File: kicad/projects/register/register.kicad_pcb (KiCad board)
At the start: 2 copper layers, 165.1 x 50.8 mm, 22 parts, among them J1 LEFT IN, J10 RIGHT LEDS, J2 LEFT OUT, J3 LEFT CONTENT, J4 BUS, J5 LEFT LEDS, J6 BACKPLANE, J7 RIGHT IN, J8 RIGHT OUT, J9 RIGHT CONTENT, U1 74HCT377, U2 74HCT245, U3 74HCT377, U4 74HCT245, U5 74HCT04

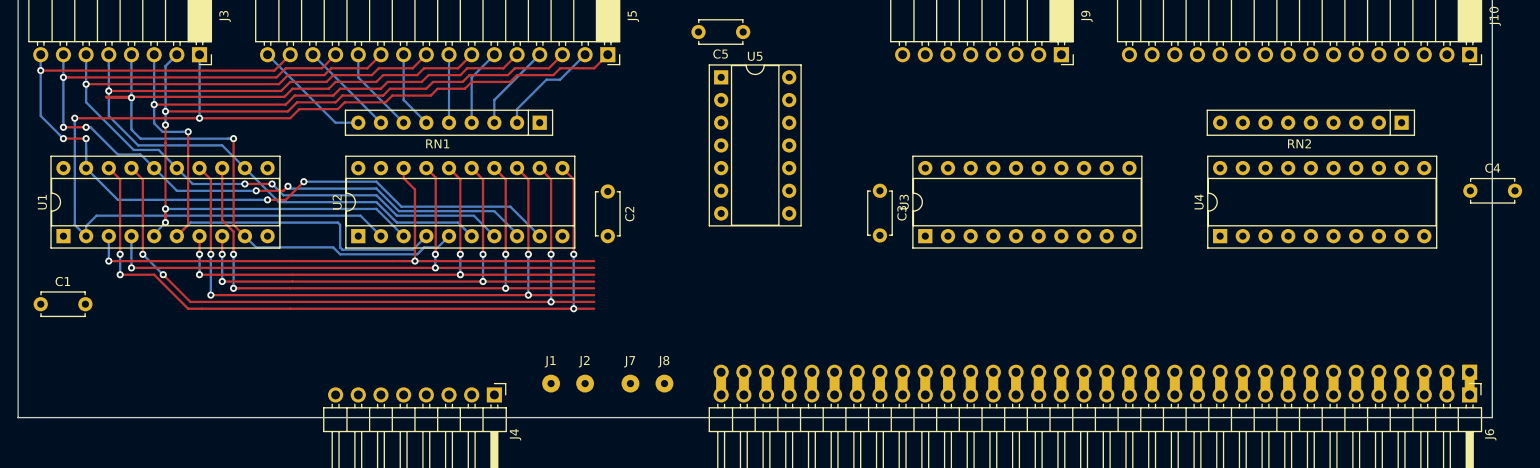
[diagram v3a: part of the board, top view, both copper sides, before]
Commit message: Add power and control signals.
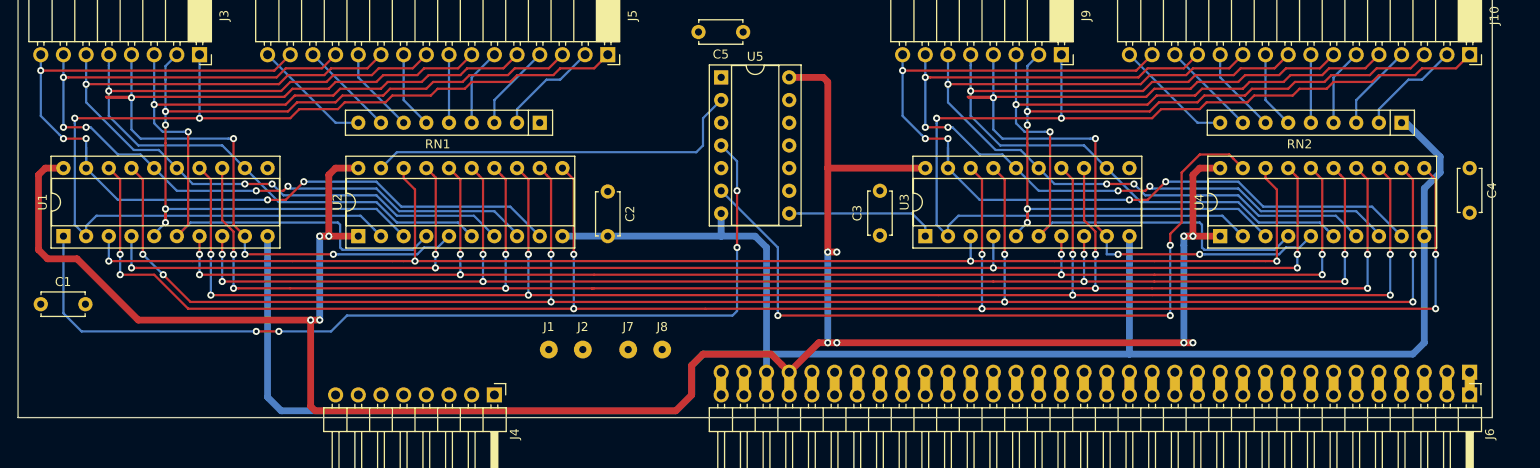
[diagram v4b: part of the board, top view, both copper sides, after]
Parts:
- moved J7 3.82 mm to (131.8, 119.4)
- moved J2 3.82 mm to (126.7, 119.4)
- moved J1 3.82 mm to (122.9, 119.4)
- moved J8 3.82 mm to (135.6, 119.4)
- moved C4 2.54 mm to (226.1, 99.1), turned to 270 degrees
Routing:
- net VCC: track 0.00 -> 259.8 mm, vias 0 -> 12
- net GND: track 0.00 -> 233.9 mm
- net /BUS_7: track 83.4 -> 210.2 mm, vias 4 -> 8
- net /BUS_6: track 78.4 -> 201.2 mm, vias 4 -> 8
- net Net-(J10-Pad1): track 0.00 -> 119.1 mm, vias 0 -> 2
- net /BUS_5: track 72.4 -> 191.1 mm, vias 4 -> 8
- net /BUS_4: track 68.4 -> 183.2 mm, vias 4 -> 8
- net Net-(U1-Pad1): track 0.00 -> 105.1 mm, vias 0 -> 4
- net Net-(J10-Pad7): track 0.00 -> 103.2 mm, vias 0 -> 4
- net Net-(J10-Pad15): track 0.00 -> 103.1 mm, vias 0 -> 5
- net /BUS_3: track 60.0 -> 162.3 mm, vias 4 -> 8
- net Net-(J10-Pad5): track 0.00 -> 99.0 mm, vias 0 -> 2
- net /BUS_2: track 61.0 -> 159.3 mm, vias 4 -> 8
- net Net-(J10-Pad3): track 0.00 -> 97.9 mm, vias 0 -> 4
- net Net-(J10-Pad13): track 0.00 -> 96.1 mm, vias 0 -> 5
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
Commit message: First version of register.
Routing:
- net /D_CLK: track 0.00 -> 151.0 mm, vias 0 -> 4
- net GND: track 233.9 -> 349.5 mm, vias 0 -> 1
- net VCC: track 259.8 -> 340.0 mm, vias 12 -> 15
- net Net-(J2-Pad1): track 0.00 -> 39.1 mm, vias 0 -> 2
- net Net-(J1-Pad1): track 0.00 -> 33.8 mm, vias 0 -> 2
- net Net-(J7-Pad1): track 0.00 -> 32.8 mm, vias 0 -> 2
- net Net-(J8-Pad1): track 0.00 -> 24.7 mm, vias 0 -> 2
- net /BUS_0: track 158.3 -> 173.3 mm, vias 4 -> 5
- net /BUS_1: track 160.9 -> 175.1 mm, vias 6 -> 7
- net /BUS_2: track 159.3 -> 172.8 mm, vias 8 -> 9
- net /BUS_3: track 162.3 -> 175.0 mm, vias 8 -> 9
- net /BUS_4: track 183.2 -> 195.1 mm, vias 8 -> 9
- net /BUS_5: track 191.1 -> 202.3 mm, vias 8 -> 9
- net /BUS_6: track 201.2 -> 211.6 mm, vias 8 -> 9
- net /BUS_7: track 210.2 -> 220.4 mm, vias 8 -> 9
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
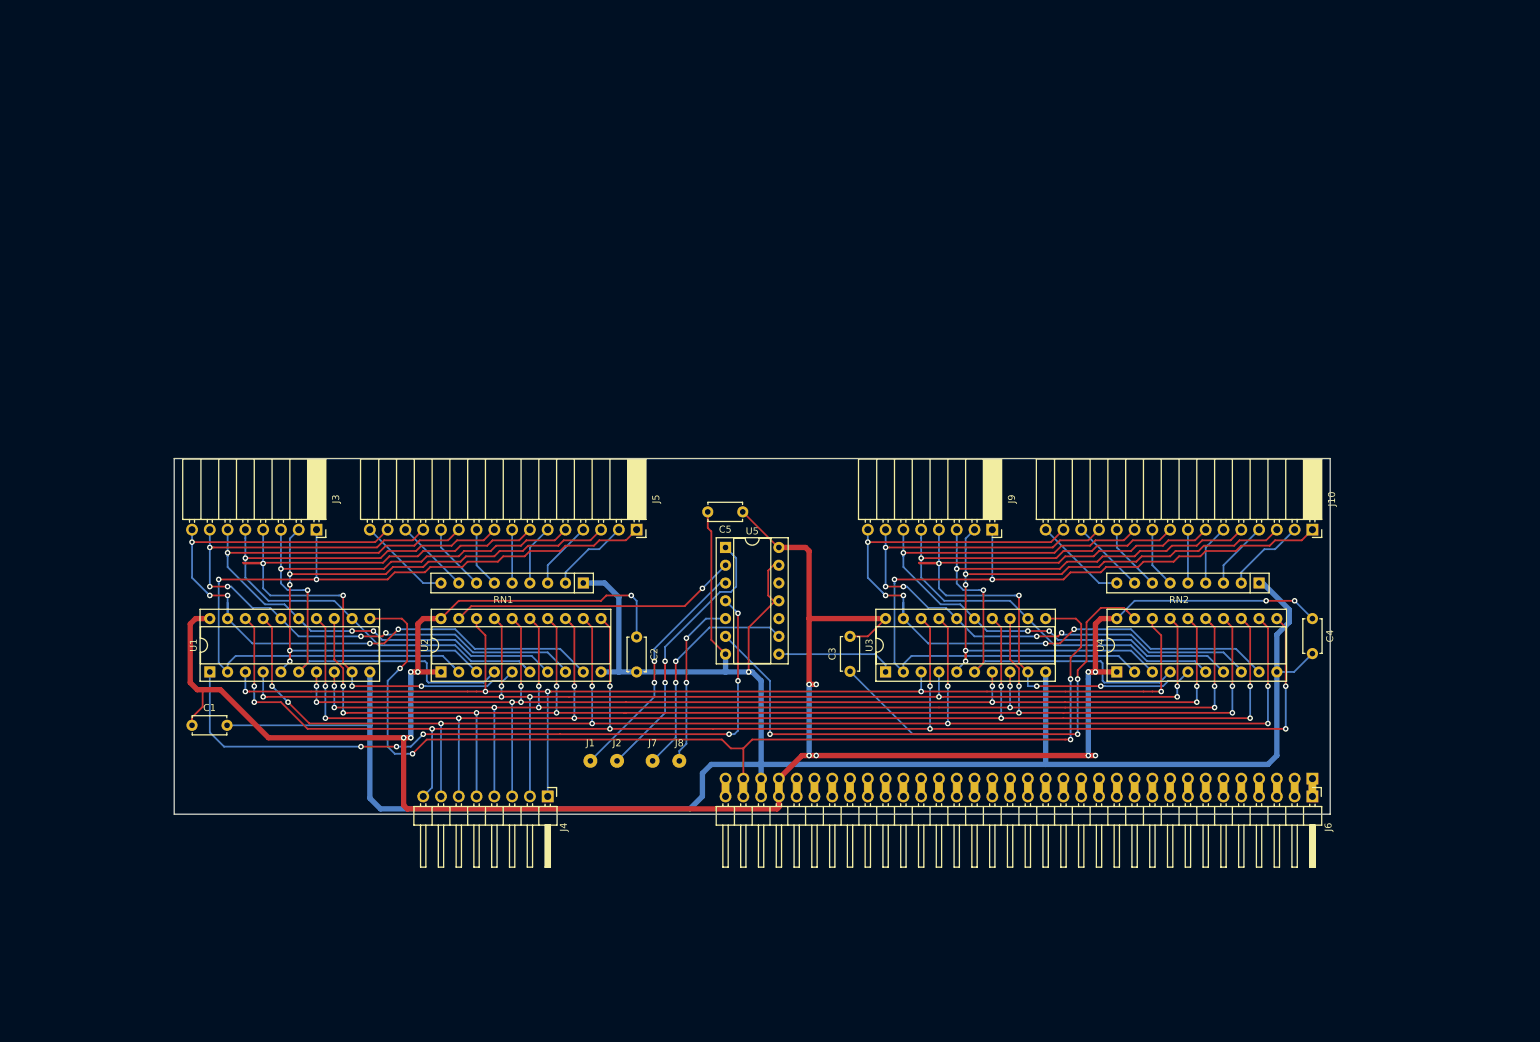
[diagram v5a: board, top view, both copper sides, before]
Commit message: Start control unit - make board slightly larger to accomodate control unit and ALU needs.
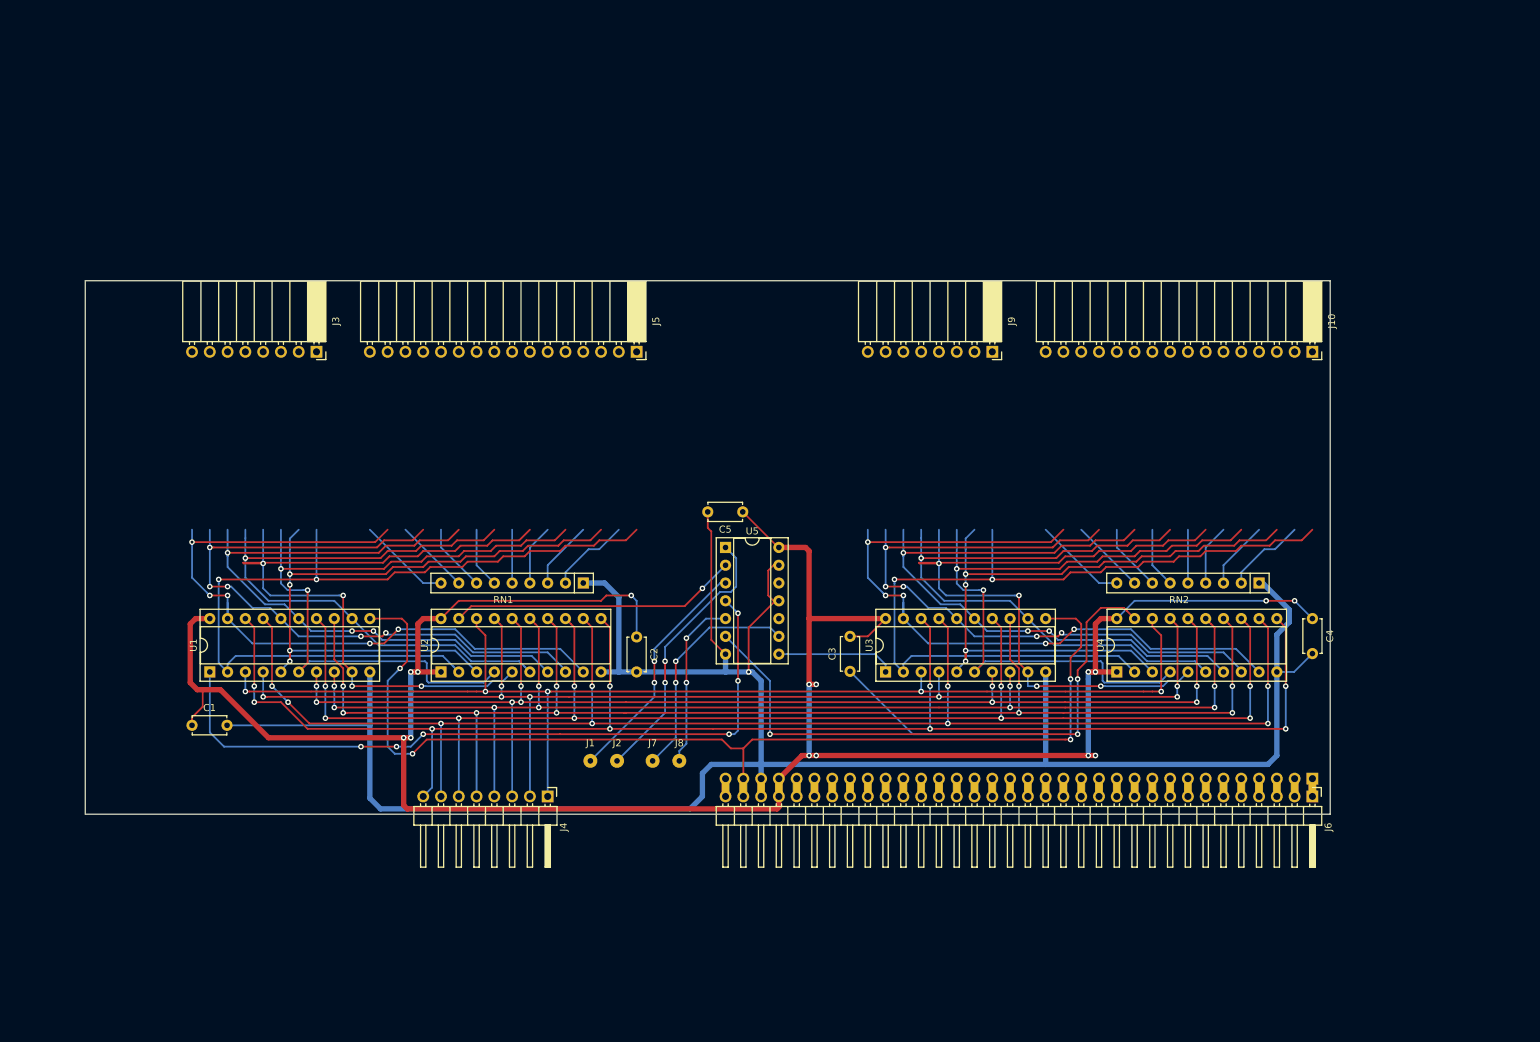
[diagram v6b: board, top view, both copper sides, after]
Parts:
- moved J10 25.4 mm to (226.1, 61.0)
- moved J3 25.4 mm to (83.8, 61.0)
- moved J5 25.4 mm to (129.5, 61.0)
- moved J9 25.4 mm to (180.3, 61.0)
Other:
- board size 165.1 x 50.8 mm -> 177.8 x 76.2 mm
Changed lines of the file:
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@@
   )
   (module Connector_PinSocket_2.54mm:PinSocket_1x16_P2.54mm_Horizontal (layer F.Cu)
-    (at 226.06 86.36 270)
+    (at 226.06 60.96 270)
     (descr "Through hole angled socket strip, 1x16, 2.54mm pitch, 8.51mm socket length, single row (from Kicad 4.0.7), script generated")
     (tags "Through hole angled socket strip THT 1x16 2.54mm single row")
@@
   )
   (module Connector_PinSocket_2.54mm:PinSocket_1x08_P2.54mm_Horizontal (layer F.Cu)
-    (at 180.34 86.36 270)
+    (at 180.34 60.96 270)
     (descr "Through hole angled socket strip, 1x08, 2.54mm pitch, 8.51mm socket length, single row (from Kicad 4.0.7), script generated")
     (tags "Through hole angled socket strip THT 1x08 2.54mm single row")
@@
   )
   (module Connector_PinSocket_2.54mm:PinSocket_1x16_P2.54mm_Horizontal (layer F.Cu)
-    (at 129.54 86.36 270)
+    (at 129.54 60.96 270)
     (descr "Through hole angled socket strip, 1x16, 2.54mm pitch, 8.51mm socket length, single row (from Kicad 4.0.7), script generated")
     (tags "Through hole angled socket strip THT 1x16 2.54mm single row")
@@
   )
   (module Connector_PinSocket_2.54mm:PinSocket_1x08_P2.54mm_Horizontal (layer F.Cu)
-    (at 83.82 86.36 270)
+    (at 83.82 60.96 270)
     (descr "Through hole angled socket strip, 1x08, 2.54mm pitch, 8.51mm socket length, single row (from Kicad 4.0.7), script generated")
     (tags "Through hole angled socket strip THT 1x08 2.54mm single row")
@@
     )
   )
-  (gr_line (start 63.5 127) (end 63.5 76.2) (layer Edge.Cuts) (width 0.05))
-  (gr_line (start 228.6 127) (end 63.5 127) (layer Edge.Cuts) (width 0.05))
-  (gr_line (start 228.6 76.2) (end 228.6 127) (layer Edge.Cuts) (width 0.05))
-  (gr_line (start 63.5 76.2) (end 228.6 76.2) (layer Edge.Cuts) (width 0.05))
+  (gr_line (start 50.8 127) (end 50.8 50.8) (layer Edge.Cuts) (width 0.05))
+  (gr_line (start 228.6 127) (end 50.8 127) (layer Edge.Cuts) (width 0.05))
+  (gr_line (start 228.6 50.8) (end 228.6 127) (layer Edge.Cuts) (width 0.05))
+  (gr_line (start 50.8 50.8) (end 228.6 50.8) (layer Edge.Cuts) (width 0.05))
   (segment (start 142.24 104.14) (end 142.24 106.68) (width 0.762) (layer B.Cu) (net 1))
   (segment (start 142.24 106.68) (end 145.542 106.68) (width 0.762) (layer B.Cu) (net 1))

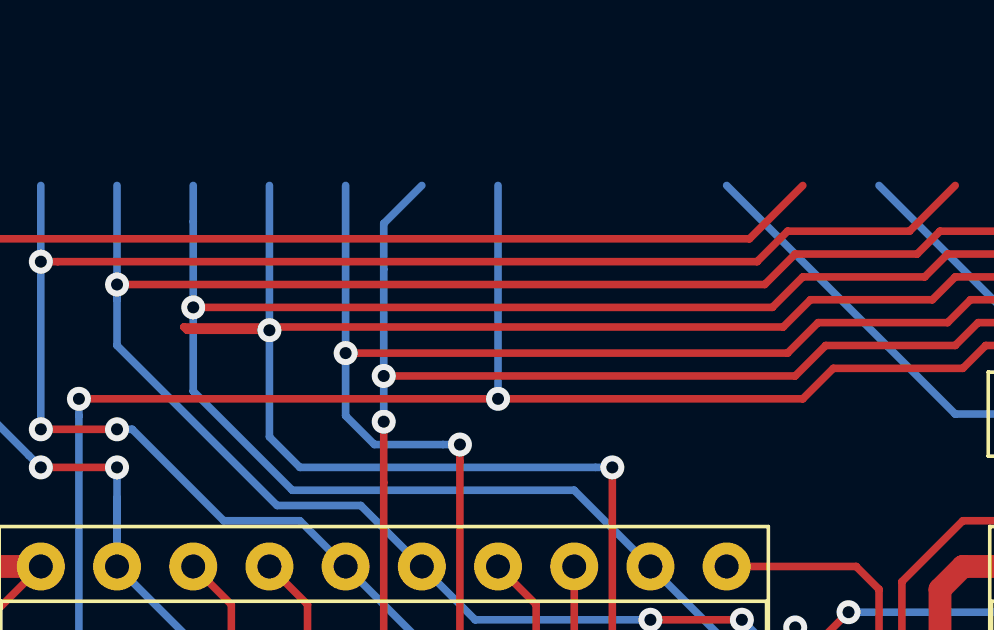
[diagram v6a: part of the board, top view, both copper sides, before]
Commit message: Start pcblayout on cu. Fix small path messiness on register.
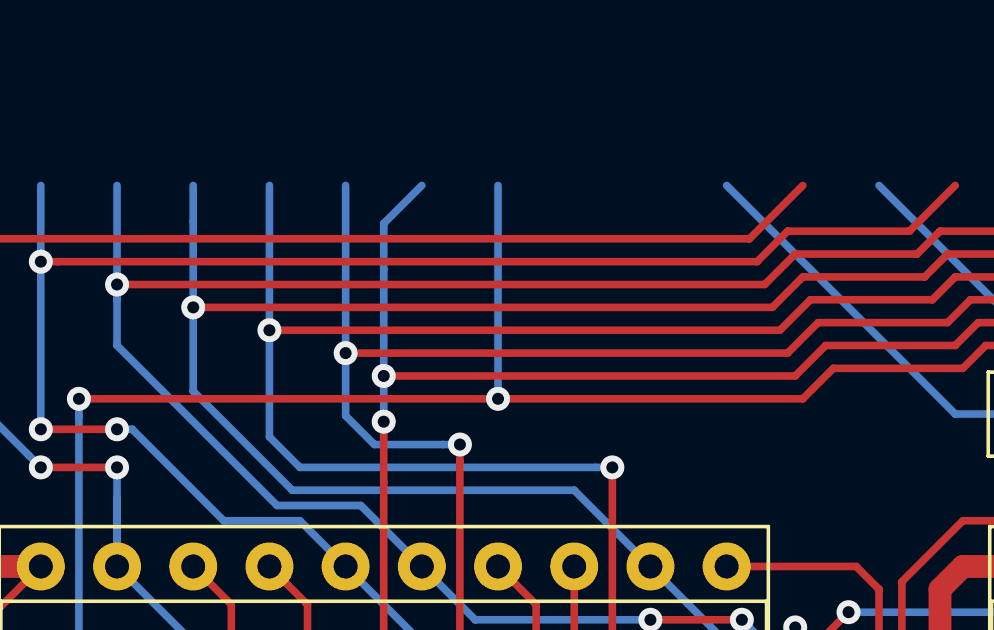
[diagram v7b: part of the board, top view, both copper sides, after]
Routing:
- net Net-(J10-Pad7): track 103.2 -> 97.5 mm
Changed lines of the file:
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@@
     (thickness 1.6)
     (drawings 4)
-    (tracks 931)
+    (tracks 929)
     (zones 0)
     (modules 22)
@@
   (via (at 172.72 91.186) (size 0.8) (drill 0.4) (layers F.Cu B.Cu) (net 64))
   (segment (start 172.72 91.186) (end 172.72 86.36) (width 0.254) (layer B.Cu) (net 64))
-  (segment (start 190.754 90.17) (end 194.818 90.17) (width 0.254) (layer F.Cu) (net 64))
-  (segment (start 209.296 87.884) (end 210.82 86.36) (width 0.254) (layer F.Cu) (net 64))
-  (segment (start 189.845999 91.078001) (end 190.754 90.17) (width 0.254) (layer F.Cu) (net 64))
-  (segment (start 195.58 89.408) (end 200.152 89.408) (width 0.254) (layer F.Cu) (net 64))
   (segment (start 184.15 105.41) (end 184.15 95.758) (width 0.254) (layer F.Cu) (net 64))
   (segment (start 173.736 95.758) (end 183.584315 95.758) (width 0.254) (layer B.Cu) (net 64))
-  (segment (start 169.974078 91.186) (end 169.866079 91.078001) (width 0.254) (layer F.Cu) (net 64))
-  (segment (start 169.866079 91.078001) (end 189.845999 91.078001) (width 0.254) (layer F.Cu) (net 64))
-  (segment (start 200.914 88.646) (end 204.724 88.646) (width 0.254) (layer F.Cu) (net 64))
   (segment (start 185.42 106.68) (end 184.15 105.41) (width 0.254) (layer F.Cu) (net 64))
-  (segment (start 205.486 87.884) (end 209.296 87.884) (width 0.254) (layer F.Cu) (net 64))
   (segment (start 183.584315 95.758) (end 184.15 95.758) (width 0.254) (layer B.Cu) (net 64))
-  (segment (start 200.152 89.408) (end 200.914 88.646) (width 0.254) (layer F.Cu) (net 64))
-  (segment (start 204.724 88.646) (end 205.486 87.884) (width 0.254) (layer F.Cu) (net 64))
   (segment (start 172.72 91.186) (end 172.72 94.742) (width 0.254) (layer B.Cu) (net 64))
   (segment (start 172.72 94.742) (end 173.736 95.758) (width 0.254) (layer B.Cu) (net 64))
-  (segment (start 194.818 90.17) (end 195.58 89.408) (width 0.254) (layer F.Cu) (net 64))
-  (segment (start 172.72 91.186) (end 169.974078 91.186) (width 0.254) (layer F.Cu) (net 64))
   (segment (start 185.42 106.68) (end 185.42 108.712) (width 0.254) (layer B.Cu) (net 64))
   (segment (start 185.42 108.712) (end 186.69 108.712) (width 0.254) (layer B.Cu) (net 64))
@@
   (segment (start 205.486 107.95) (end 204.724 108.712) (width 0.254) (layer B.Cu) (net 64))
   (segment (start 207.01 107.95) (end 205.486 107.95) (width 0.254) (layer B.Cu) (net 64))
+  (segment (start 204.724 88.646) (end 205.486 87.884) (width 0.254) (layer F.Cu) (net 64))
+  (segment (start 200.914 88.646) (end 204.724 88.646) (width 0.254) (layer F.Cu) (net 64))
+  (segment (start 200.152 89.408) (end 200.914 88.646) (width 0.254) (layer F.Cu) (net 64))
+  (segment (start 189.738 91.186) (end 190.754 90.17) (width 0.254) (layer F.Cu) (net 64))
+  (segment (start 190.754 90.17) (end 194.818 90.17) (width 0.254) (layer F.Cu) (net 64))
+  (segment (start 205.486 87.884) (end 209.296 87.884) (width 0.254) (layer F.Cu) (net 64))
+  (segment (start 172.72 91.186) (end 189.738 91.186) (width 0.254) (layer F.Cu) (net 64))
+  (segment (start 194.818 90.17) (end 195.58 89.408) (width 0.254) (layer F.Cu) (net 64))
+  (segment (start 209.296 87.884) (end 210.82 86.36) (width 0.254) (layer F.Cu) (net 64))
+  (segment (start 195.58 89.408) (end 200.152 89.408) (width 0.254) (layer F.Cu) (net 64))
   (via (at 175.26 91.948) (size 0.8) (drill 0.4) (layers F.Cu B.Cu) (net 65))
   (via (at 179.069994 94.996) (size 0.8) (drill 0.4) (layers F.Cu B.Cu) (net 65))

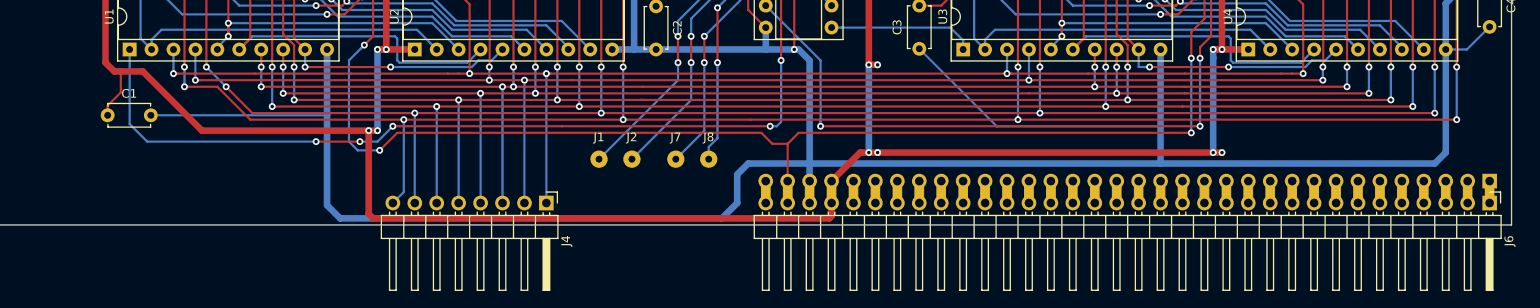
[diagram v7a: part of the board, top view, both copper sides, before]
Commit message: Add bus and aux symbols. Update backplane footprint and 3dmodel. Update register PCB to use new footprints.
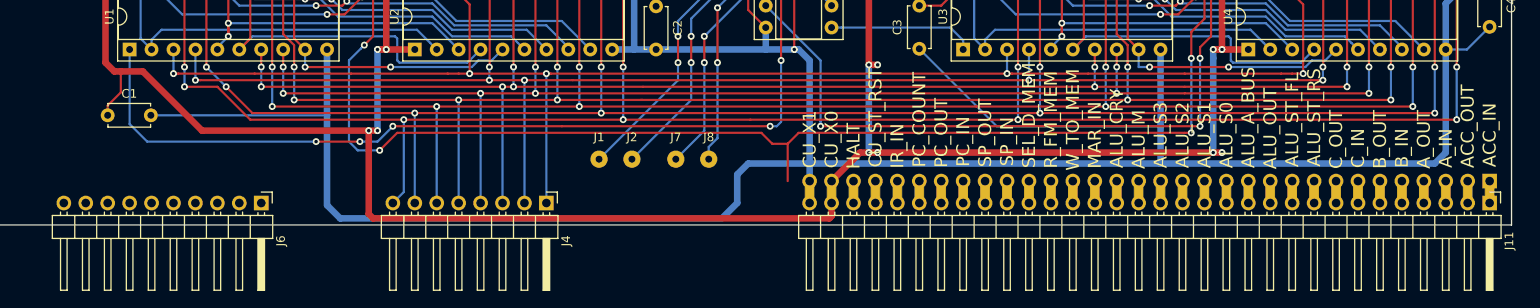
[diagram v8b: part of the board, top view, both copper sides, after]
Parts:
- added J11: Control_signal_backplane, eight-bit-computer:backplane-connector, F.Cu at (226.1, 124.5)
- J6: value BACKPLANE -> Aux_connection; footprint eight-bit-computer:backplane-connector -> Connector_PinHeader_2.54mm:PinHeader_1x10_P2.54mm_Horizontal
- moved J6 142.2 mm to (83.8, 124.5)
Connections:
- J6 pad 1: Net-(J6-Pad1) -> VCC
- J6 pad 2: Net-(J6-Pad2) -> VCC
- J6 pad 3: Net-(J6-Pad3) -> GND
- J6 pad 4: Net-(J6-Pad4) -> GND
- J6 pad 6: Net-(J6-Pad6) -> /D_CLK
